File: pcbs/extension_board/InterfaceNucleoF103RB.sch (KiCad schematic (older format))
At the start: 9 parts, among them J6 Conn_02x19_Odd_Even, J7 Conn_02x19_Odd_Even

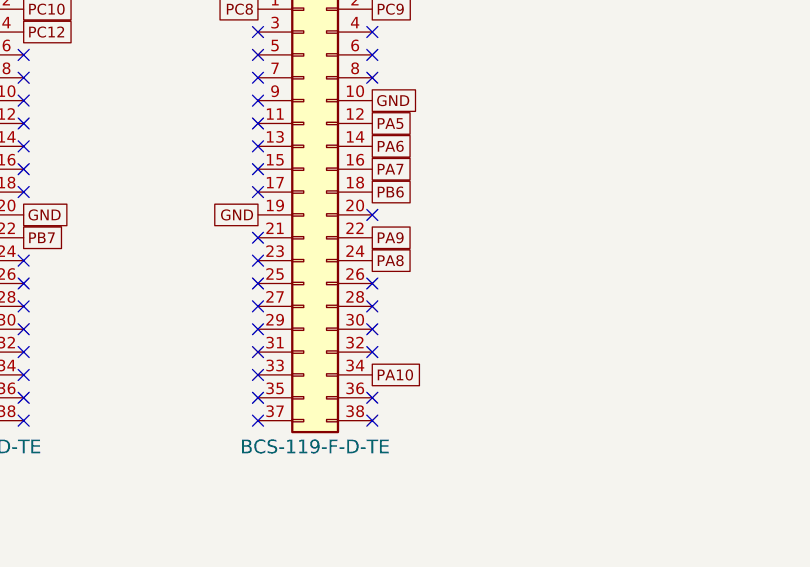
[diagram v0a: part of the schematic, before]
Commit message: osPrintf works with signed and unsigned integers.
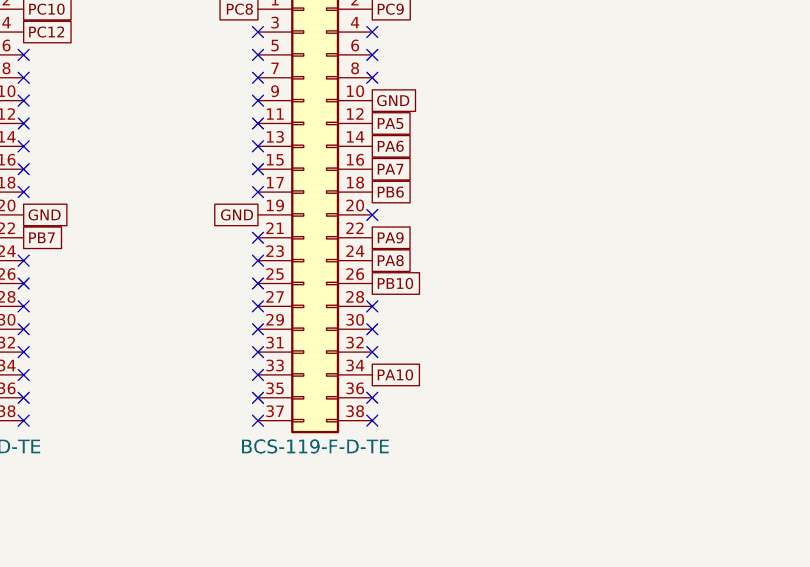
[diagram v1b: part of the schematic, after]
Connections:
- net PB10: now reaches J7.26 (Pin_26)
- no-connect marks 54 -> 53
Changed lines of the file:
@@
 NoConn ~ 4155 3765
 NoConn ~ 4155 3665
-NoConn ~ 4655 3865
 NoConn ~ 4655 3965
 NoConn ~ 4655 4065
@@
 Text GLabel 4655 3265 2    47   UnSpc ~ 0
 PA6
+Text GLabel 4655 3865 2    47   UnSpc ~ 0
+PB10
 $EndSCHEMATC
